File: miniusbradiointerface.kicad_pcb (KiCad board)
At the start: 2 copper layers, 17 x 16 mm, 22 parts, among them J1 VCC, J2 DP, J3 DM, J4 GND, J5 DB9_Male, Q1 BSS138, U1 CM108AH, Y1 12M

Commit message: KiCad 6 migration
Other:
- net class Default removed

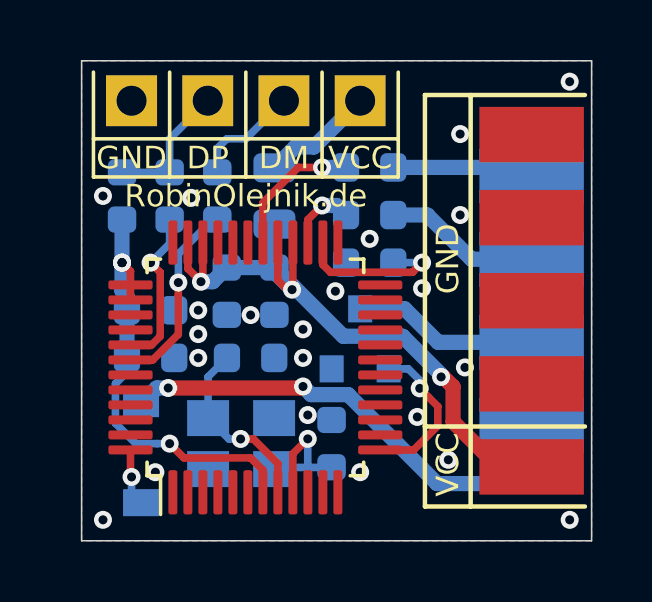
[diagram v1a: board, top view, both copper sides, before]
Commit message: Update project to KiCad 8
Some symbols and footprints were updated and/or renamed in the library.
Update the symbols, keep the footprints. Fix ERC and DRC errors.
Update website URL and version
Update PDF schematic
Update ibom, add config file
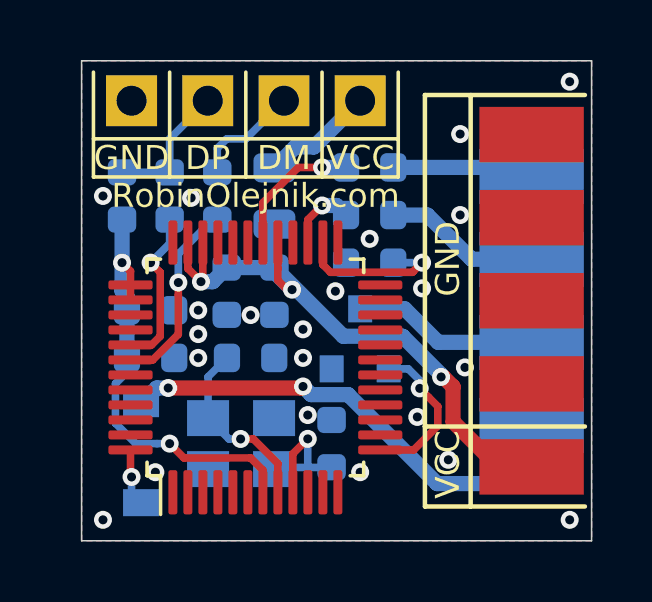
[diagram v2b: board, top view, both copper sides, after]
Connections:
- U1 pad 1: (no net) -> unconnected-(U1-SPDIFO-Pad1)
- U1 pad 11: (no net) -> unconnected-(U1-GPIO2-Pad11)
- U1 pad 12: (no net) -> unconnected-(U1-LED0-Pad12)
- U1 pad 15: (no net) -> unconnected-(U1-GPIO4-Pad15)
- U1 pad 16: (no net) -> unconnected-(U1-SDIN-Pad16)
- U1 pad 17: (no net) -> unconnected-(U1-ADSCLK-Pad17)
- U1 pad 18: (no net) -> unconnected-(U1-MUTEP-Pad18)
- U1 pad 19: (no net) -> unconnected-(U1-ADLRCK-Pad19)
- U1 pad 2: (no net) -> unconnected-(U1-DI-Pad2)
- U1 pad 20: (no net) -> unconnected-(U1-ADMCLK-Pad20)
- U1 pad 21: (no net) -> unconnected-(U1-LEDR-Pad21)
- U1 pad 25: (no net) -> unconnected-(U1-VBIAS-Pad25)
- U1 pad 28: VCC -> unconnected-(U1-N.C.-Pad28)
- U1 pad 3: (no net) -> unconnected-(U1-DO-Pad3)
- U1 pad 31: (no net) -> unconnected-(U1-LOBS-Pad31)
- U1 pad 32: (no net) -> unconnected-(U1-LOR-Pad32)
- U1 pad 39: (no net) -> unconnected-(U1-VOLUP-Pad39)
- U1 pad 4: (no net) -> unconnected-(U1-SK-Pad4)
- U1 pad 40: (no net) -> unconnected-(U1-PDSW-Pad40)
- U1 pad 43: (no net) -> unconnected-(U1-GPIO1-Pad43)
- U1 pad 44: (no net) -> unconnected-(U1-SDOUT-Pad44)
- U1 pad 45: (no net) -> unconnected-(U1-DAMCLK-Pad45)
- U1 pad 46: (no net) -> unconnected-(U1-DALRCK-Pad46)
- U1 pad 47: (no net) -> unconnected-(U1-DASCLK-Pad47)
- U1 pad 5: (no net) -> unconnected-(U1-CSO-Pad5)
- U1 pad 6: (no net) -> unconnected-(U1-MUTER-Pad6)
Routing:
- net VCC: track 25.1 -> 23.6 mm
- net +3V3: vias 3 -> 2
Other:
- board text added: "RobinOlejnik.com"
- board text added: "V0.1.1"
- board text removed: "RobinOlejnik.de"
- board text removed: "V0.1.0"
